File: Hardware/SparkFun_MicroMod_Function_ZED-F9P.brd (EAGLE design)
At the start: 38 x 65 mm, 112 parts, among them J1 USB Female Type C Connector, J10 U.FL, J11 455-1750-1-ND, J15 QWIIC_VERT, J16 QWIIC_RA, J18 Bus Selection, J2 MICROMOD_STANDARD, J3 Bus Selection, Q1 DMP21D0UT, U1 SN74LVC1G66DRYR, U10 SN74AUP1T04DCK, U11 SN74AUP1T04DCK, U2 3.3V, U3 EEPROM, U4 74LVC4066D_QUAD_BILATERAL_SWI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, U5 74LVC4066D_QUAD_BILATERAL_SWI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, U6 OPA344, U7 74LVC541ABQ, U8 U-BLOX_ZED-F9P, U9 FIN1017MXSOIC-8

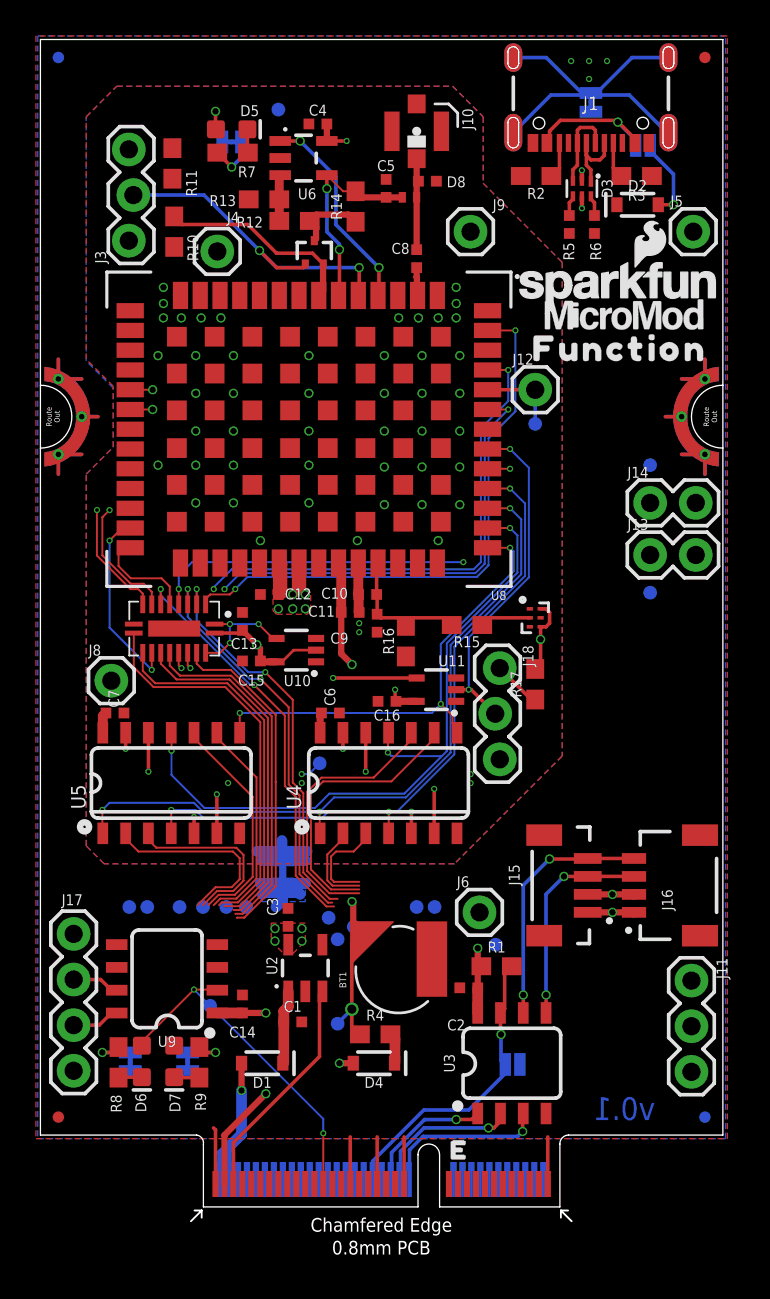
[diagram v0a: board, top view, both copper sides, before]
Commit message: All traces routed.
All traces routed, now need to just finish up via stitching, grounding, then silks.
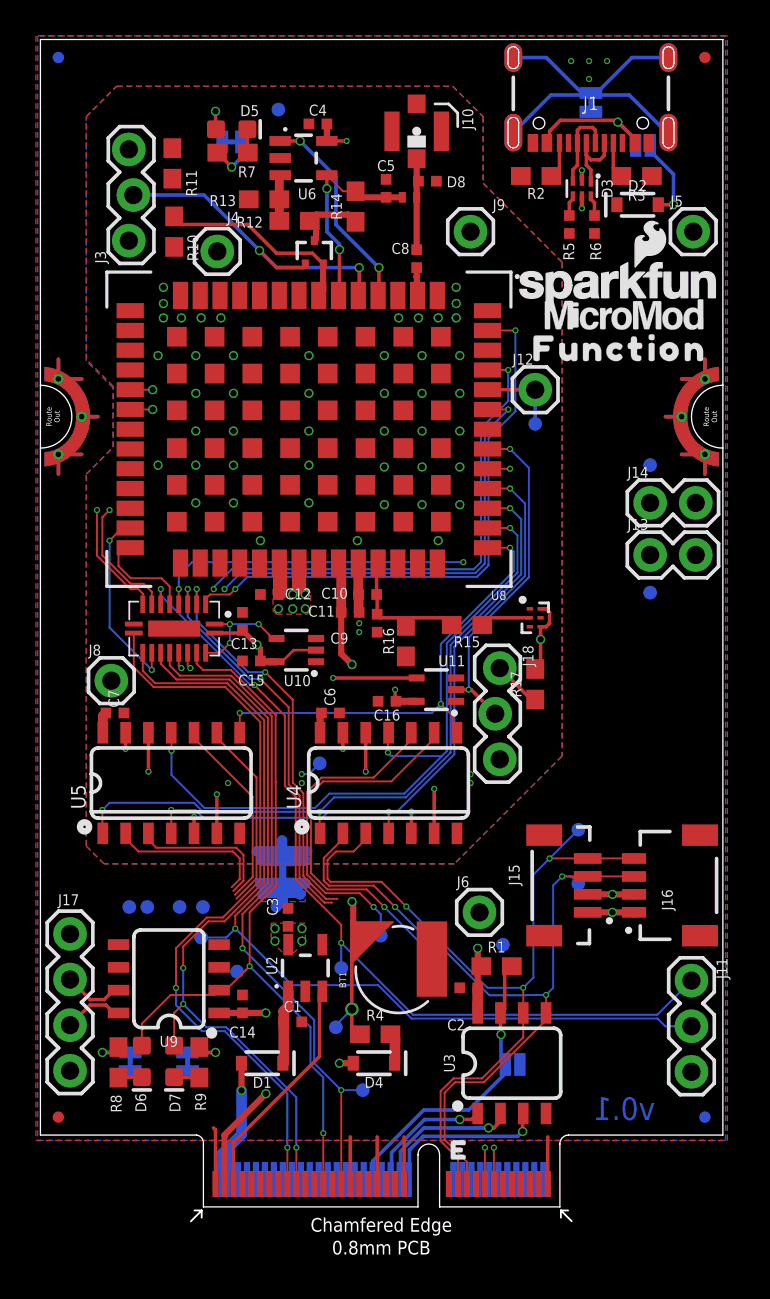
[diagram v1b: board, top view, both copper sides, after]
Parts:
- BT1: value ML414H_IV01E_BATTERY -> RELOWABLE_BATTERY_MS421R; device SparkFun-Batteries:ML414H_IV01E -> SparkFun-Batteries:MS421R_IV03E
- moved TP6 14.0 mm to (30.0, 18.0)
- moved TP5 13.6 mm to (30.0, 21.0)
- moved TP14 8.52 mm to (18.0, 6.50)
- moved TP15 7.25 mm to (16.8, 13.3)
- moved TP8 3.10 mm to (22.1, 13.6)
- moved TP16 3.02 mm to (9.00, 15.0)
- moved TP7 2.56 mm to (19.0, 15.1)
- moved TP9 2.42 mm to (11.0, 13.1)
- moved TP2 0.40 mm to (25.8, 14.6)
- moved TP3 0.22 mm to (16.5, 10.0)
- moved J17 0.20 mm to (1.70, 15.2)
- moved U9 0.10 mm to (7.20, 12.7)
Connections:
- net GEO_STAT: now also J2.59; no longer J2.57
- net RTK_STAT: now also J2.57; no longer J2.59
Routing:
- net TX2/RTCM: track 19.6 -> 50.1 mm, vias 0 -> 1
- net MM_SDA: track 16.8 -> 44.5 mm, vias 2 -> 3
- net MM_SCL: track 19.3 -> 46.3 mm, vias 2 -> 3
- net RX2/RTCM: track 22.9 -> 48.2 mm, vias 2 -> 3
- net MM_TX: track 15.8 -> 40.4 mm, vias 0 -> 2
- net RTK_STAT: track 20.7 -> 42.9 mm, vias 0 -> 3
- net MM_RX: track 15.2 -> 36.9 mm, vias 0 -> 2
- net GEO_STAT: track 21.9 -> 41.7 mm, vias 0 -> 2
- net TX_READY: track 19.6 -> 37.8 mm, vias 0 -> 2
- net PPS: track 38.1 -> 44.0 mm
- net MM_!CS!: track 11.2 -> 8.90 mm
- net MM_SCK: track 10.3 -> 8.25 mm
- net MM_COPI: track 12.5 -> 10.8 mm
- net MM_CIPO: track 12.0 -> 10.6 mm
- net PPS_DIFF_P: track 2.65 -> 3.38 mm
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
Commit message: Change net class for vbatt.
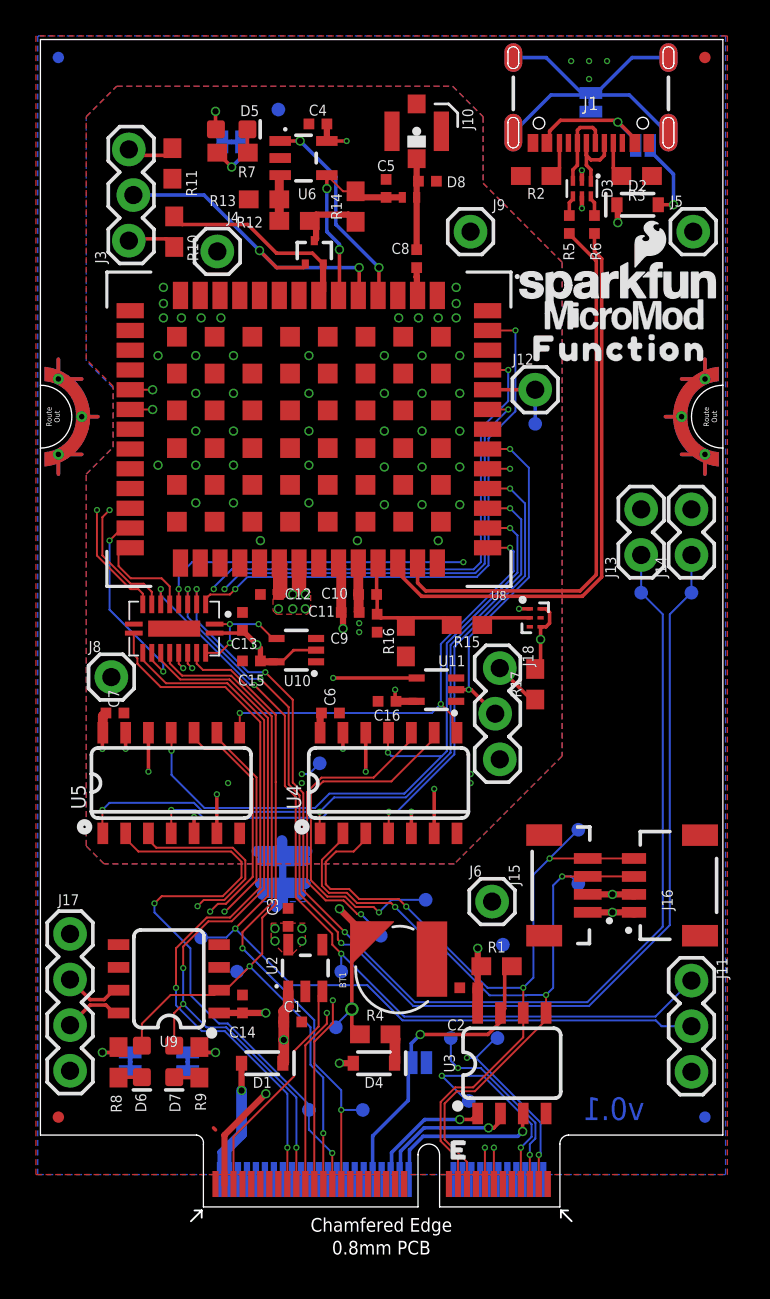
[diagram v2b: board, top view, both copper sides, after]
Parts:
- moved TP10 20.8 mm to (25.5, 9.40)
- moved TP13 18.3 mm to (23.9, 5.90)
- moved TP12 16.8 mm to (22.9, 9.40)
- moved TP11 15.1 mm to (15.0, 5.40)
- moved TP19 7.46 mm to (36.3, 34.2)
- moved JP2 5.20 mm to (21.1, 8.03)
- moved J14 3.70 mm to (36.3, 36.3), turned to 90 degrees
- moved TP8 3.55 mm to (21.5, 17.1)
- moved TP14 1.10 mm to (18.0, 5.40)
- moved J6 0.92 mm to (25.2, 17.0)
- moved J13 0.50 mm to (33.5, 36.3), turned to 90 degrees
- moved TP18 0.50 mm to (33.5, 34.2)
- moved TP15 0.20 mm to (16.8, 13.1)
- moved J8 0.20 mm to (4.00, 29.5)
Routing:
- net EXTINT: track 22.3 -> 81.8 mm, vias 2 -> 4
- net 5V: track 4.12 -> 63.2 mm, vias 0 -> 2
- net !RESET!: track 22.3 -> 81.2 mm, vias 2 -> 4
- net MM_SCK: track 8.25 -> 44.5 mm, vias 0 -> 3
- net MM_COPI: track 10.8 -> 44.8 mm, vias 0 -> 3
- net ZED_USB_N: track 0.00 -> 32.2 mm
- net MM_CIPO: track 10.6 -> 42.2 mm, vias 0 -> 3
- net ZED_USB_P: track 0.00 -> 31.2 mm
- net V_USB: track 14.4 -> 41.0 mm, vias 2 -> 3
- net MM_!CS!: track 8.90 -> 33.6 mm, vias 0 -> 2
- net GND: track 23.0 -> 9.49 mm
- net N$11: track 0.00 -> 2.75 mm
- net N$12: track 0.00 -> 2.73 mm
- net MM_TX: track 40.4 -> 38.5 mm
- net MM_RX: track 36.9 -> 35.7 mm
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
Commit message: GND stitching and grounding complete.
Outer GND plane stitching complete.
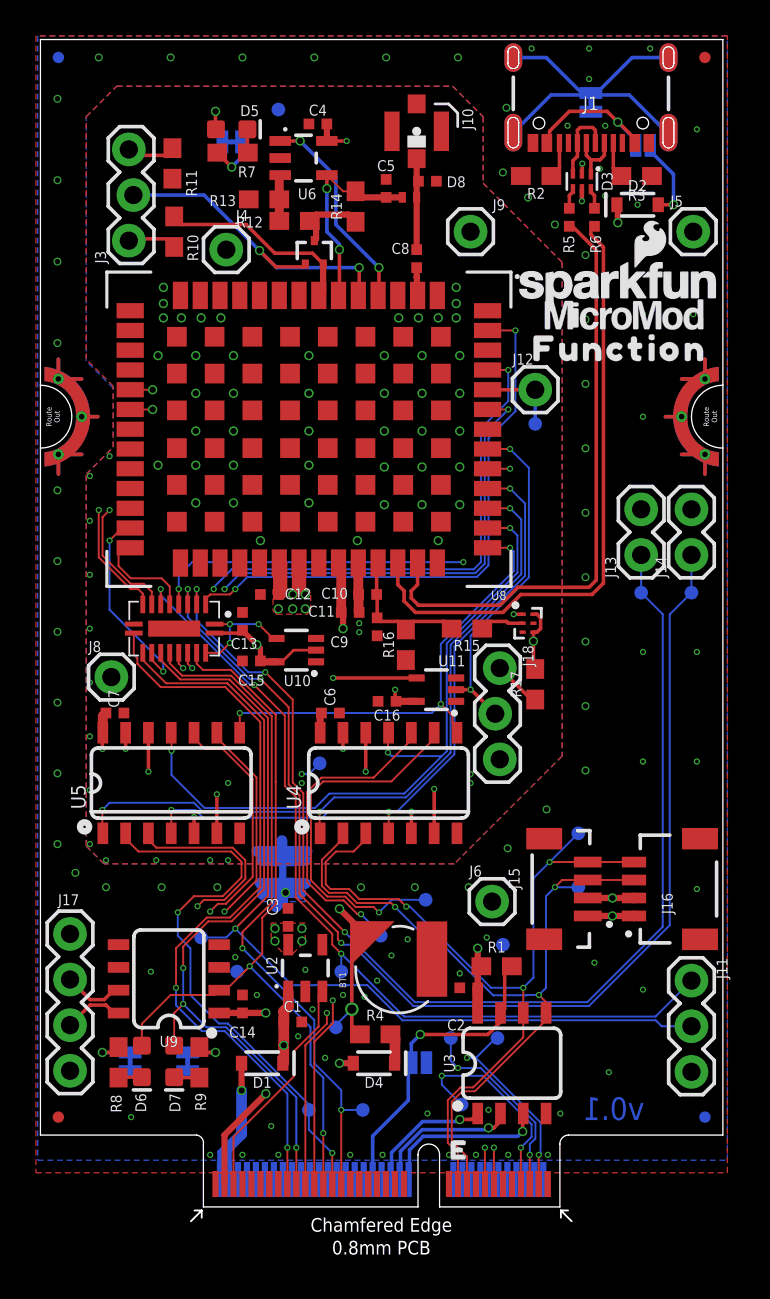
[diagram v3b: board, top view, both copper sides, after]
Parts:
- moved J4 0.51 mm to (10.4, 53.3)
- moved U1 0.50 mm to (26.9, 33.0)
- moved TP13 0.45 mm to (23.5, 5.70)
- moved D3 0.40 mm to (30.2, 57.1)
- moved R5 0.40 mm to (29.5, 55.1)
- moved R6 0.40 mm to (30.9, 55.1)
- moved C9 0.20 mm to (18.8, 32.3)
- moved J15 0.20 mm to (31.3, 17.7)
- moved J16 0.20 mm to (33.1, 17.7)
- moved R16 0.20 mm to (20.4, 31.3)
- moved TP5 0.20 mm to (30.0, 20.8)
- moved TP6 0.20 mm to (30.0, 17.8)
- moved R15 0.20 mm to (23.8, 32.2)
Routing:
- net ZED_USB_N: track 32.2 -> 34.5 mm
- net ZED_USB_P: track 31.2 -> 33.6 mm
- net MM_!CS!: track 33.6 -> 31.5 mm
- net USBC_N: track 4.83 -> 3.38 mm
- net V_USB: track 41.0 -> 42.2 mm
- net MM_SCL: track 46.3 -> 45.6 mm
- net V_ZED: track 24.4 -> 23.8 mm
- net MM_SDA: track 44.4 -> 43.9 mm
- net GND: track 9.49 -> 9.32 mm, vias 6 -> 88
- net GND_RF: vias 49 -> 62

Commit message: Stitching of GND_RF complete.
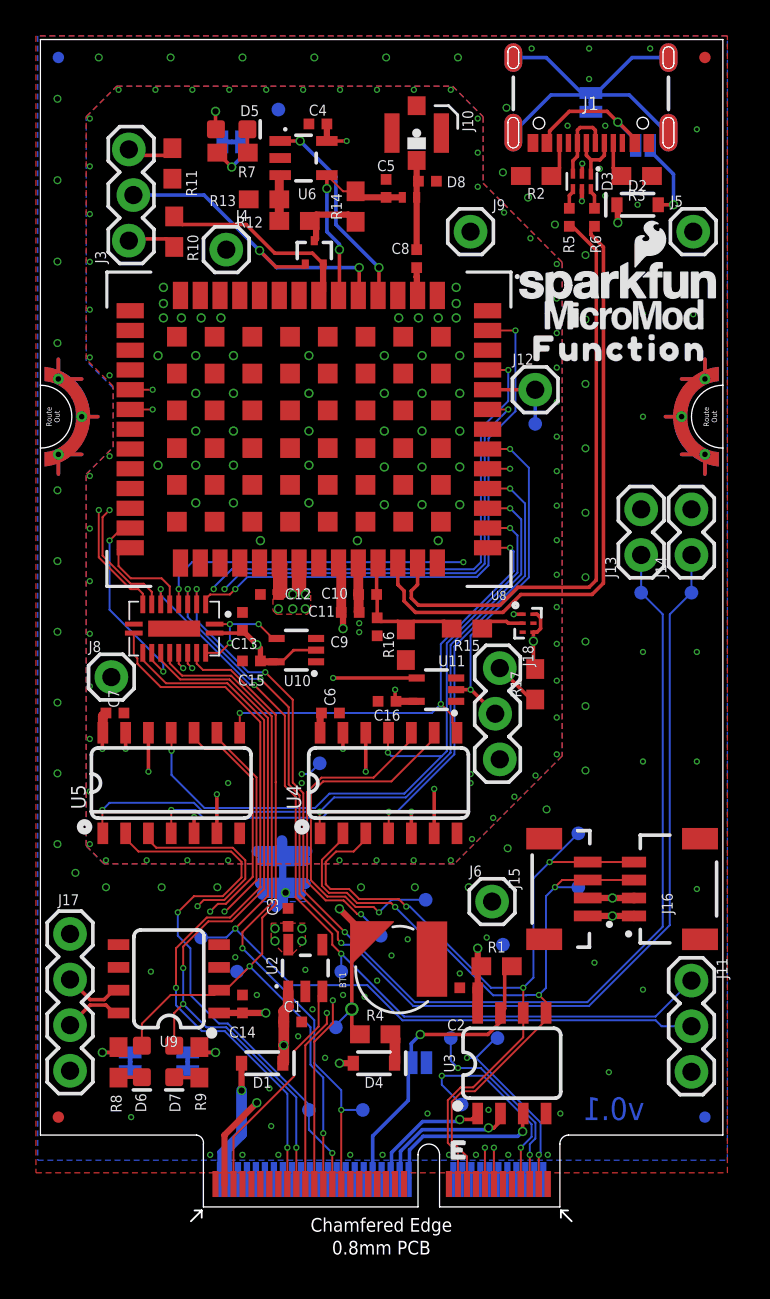
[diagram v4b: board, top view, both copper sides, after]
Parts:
- moved J10 0.10 mm to (21.0, 59.8)
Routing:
- net 3.3V: track 44.3 -> 45.9 mm
- net GND_RF: vias 62 -> 107
- net GND: vias 88 -> 89
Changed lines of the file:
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@@
 <attribute name="VALUE" x="18.362" y="55.7" size="0.6096" layer="27" font="vector" ratio="20" rot="R90" align="top-center"/>
 </element>
-<element name="J10" library="SparkFun-Connectors" package="U.FL" value="U.FL" x="21" y="59.89" smashed="yes" rot="R270">
-<attribute name="NAME" x="23.54" y="61.16" size="0.6096" layer="25" font="vector" ratio="20" rot="R270"/>
-<attribute name="PROD_ID" value="CONN-09193" x="21" y="59.89" size="1.778" layer="27" rot="R270" display="off"/>
-<attribute name="SF_ID" value="WRL-09144" x="21" y="59.89" size="1.778" layer="27" rot="R270" display="off"/>
-<attribute name="VALUE" x="18.46" y="61.16" size="0.6096" layer="27" font="vector" ratio="20" rot="R270" align="top-left"/>
+<element name="J10" library="SparkFun-Connectors" package="U.FL" value="U.FL" x="21" y="59.79" smashed="yes" rot="R270">
+<attribute name="NAME" x="23.54" y="61.06" size="0.6096" layer="25" font="vector" ratio="20" rot="R270"/>
+<attribute name="PROD_ID" value="CONN-09193" x="21" y="59.79" size="1.778" layer="27" rot="R270" display="off"/>
+<attribute name="SF_ID" value="WRL-09144" x="21" y="59.79" size="1.778" layer="27" rot="R270" display="off"/>
+<attribute name="VALUE" x="18.46" y="61.06" size="0.6096" layer="27" font="vector" ratio="20" rot="R270" align="top-left"/>
 </element>
 <element name="D8" library="SparkFun-DiscreteSemi" package="0402-TIGHT" value="PESD0402-0402T" x="21.6" y="57.11" smashed="yes">
@@
 <via x="21.6" y="5.2" extent="1-16" drill="0.2"/>
 <via x="25" y="5.4" extent="1-16" drill="0.2"/>
+<via x="12.8" y="6.6" extent="1-16" drill="0.2"/>
 </signal>
 <signal name="3.3V" class="4">
@@
 <wire x1="31.9" y1="17.2" x2="29.1" y2="14.4" width="0.35" layer="15"/>
 <wire x1="10.3" y1="1.275" x2="10.3" y2="4" width="0.35" layer="1"/>
-<wire x1="10.3" y1="4" x2="12.6" y2="6.3" width="0.35" layer="1"/>
-<via x="12.6" y="6.3" extent="1-16" drill="0.35"/>
-<wire x1="16.7" y1="8" x2="15" y2="6.3" width="0.35" layer="15"/>
-<wire x1="12.6" y1="6.3" x2="15" y2="6.3" width="0.35" layer="15"/>
-<wire x1="12.6" y1="6.3" x2="12.6" y2="10.8" width="0.35" layer="15"/>
+<wire x1="10.3" y1="4" x2="12.1" y2="5.8" width="0.35" layer="1"/>
+<via x="12.1" y="5.8" extent="1-16" drill="0.35"/>
+<wire x1="16.7" y1="8" x2="16.7" y2="6.4" width="0.35" layer="15"/>
+<wire x1="16.7" y1="6.4" x2="16.1" y2="5.8" width="0.35" layer="15"/>
+<wire x1="12.1" y1="5.8" x2="16.1" y2="5.8" width="0.35" layer="15"/>
+<wire x1="12.1" y1="10.3" x2="12.6" y2="10.8" width="0.35" layer="15"/>
+<wire x1="12.1" y1="10.3" x2="12.1" y2="5.8" width="0.35" layer="15"/>
 <via x="12.6" y="10.8" extent="1-16" drill="0.35"/>
 <wire x1="12.6" y1="10.8" x2="11.3" y2="10.8" width="0.35" layer="1"/>
@@
 <wire x1="3.51" y1="36.26346875" x2="5.07506875" y2="34.6984" width="0.11" layer="1"/>
 <wire x1="5.05" y1="44.4" x2="6.3" y2="44.4" width="0.11" layer="1"/>
-<via x="6.3" y="44.4" extent="1-16" drill="0.35"/>
+<via x="6.3" y="44.4" extent="1-16" drill="0.2"/>
 <wire x1="6.3" y1="44.4" x2="5.8116" y2="43.9116" width="0.11" layer="15"/>
 <wire x1="5.8116" y1="43.9116" x2="5.8116" y2="42.11235" width="0.11" layer="15"/>
@@
 <wire x1="5.75" y1="34.1468" x2="5.5" y2="34.3968" width="0.11" layer="1"/>
 <wire x1="5.05" y1="45.5" x2="6.3" y2="45.5" width="0.11" layer="1"/>
-<via x="6.3" y="45.5" extent="1-16" drill="0.35"/>
+<via x="6.3" y="45.5" extent="1-16" drill="0.2"/>
 <wire x1="6.3" y1="45.5" x2="5.6" y2="44.8" width="0.11" layer="15"/>
 <wire x1="3.68" y1="40.28" x2="3.68" y2="39.18" width="0.11" layer="15"/>
@@
 <vertex x="24.7" y="60.7"/>
 </polygon>
-<via x="10.5" y="19.3" extent="1-16" drill="0.2"/>
-<via x="9.5" y="19.3" extent="1-16" drill="0.2"/>
-<via x="6.5" y="19.3" extent="1-16" drill="0.2"/>
+<via x="10.499996875" y="19.3" extent="1-16" drill="0.2"/>
+<via x="8.23333125" y="19.3" extent="1-16" drill="0.2"/>
+<via x="5.966665625" y="19.3" extent="1-16" drill="0.2"/>
 <via x="3.7" y="19.3" extent="1-16" drill="0.2"/>
 <via x="2.8" y="20.2" extent="1-16" drill="0.2"/>
-<via x="2.8" y="23.2" extent="1-16" drill="0.2"/>
-<via x="2.8" y="26.2" extent="1-16" drill="0.2"/>
-<via x="2.8" y="29.2" extent="1-16" drill="0.2"/>
-<via x="2.8" y="32.2" extent="1-16" drill="0.2"/>
-<via x="2.8" y="35.2" extent="1-16" drill="0.2"/>
-<via x="2.8" y="38.2" extent="1-16" drill="0.2"/>
-<via x="2.8" y="40.7" extent="1-16" drill="0.2"/>
+<via x="2.8" y="23.12856875" extent="1-16" drill="0.2"/>
+<via x="2.8" y="26.0571375" extent="1-16" drill="0.2"/>
+<via x="2.8" y="28.98570625" extent="1-16" drill="0.2"/>
+<via x="2.8" y="31.914275" extent="1-16" drill="0.2"/>
+<via x="2.8" y="34.84284375" extent="1-16" drill="0.2"/>
+<via x="2.8" y="37.7714125" extent="1-16" drill="0.2"/>
+<via x="2.8" y="40.69998125" extent="1-16" drill="0.2"/>
 <via x="3.9" y="41.8" extent="1-16" drill="0.2"/>
+<via x="3.9" y="46.3" extent="1-16" drill="0.2"/>
+<via x="2.8" y="47.3" extent="1-16" drill="0.2"/>
+<via x="2.8" y="49.96" extent="1-16" drill="0.2"/>
+<via x="2.8" y="52.62" extent="1-16" drill="0.2"/>
+<via x="2.8" y="55.28" extent="1-16" drill="0.2"/>
+<via x="2.8" y="57.94" extent="1-16" drill="0.2"/>
+<via x="2.8" y="60.6" extent="1-16" drill="0.2"/>
+<via x="4.4" y="62.2" extent="1-16" drill="0.2"/>
+<via x="6.45555" y="62.2" extent="1-16" drill="0.2"/>
+<via x="8.5111" y="62.2" extent="1-16" drill="0.2"/>
+<via x="10.56665" y="62.2" extent="1-16" drill="0.2"/>
+<via x="12.6222" y="62.2" extent="1-16" drill="0.2"/>
+<via x="14.67775" y="62.2" extent="1-16" drill="0.2"/>
+<via x="16.7333" y="62.2" extent="1-16" drill="0.2"/>
+<via x="22.89995" y="62.2" extent="1-16" drill="0.2"/>
+<via x="18.78885" y="62.2" extent="1-16" drill="0.2"/>
+<via x="20.8444" y="62.2" extent="1-16" drill="0.2"/>
+<via x="24.4" y="60.6" extent="1-16" drill="0.2"/>
+<via x="24.4" y="58.7" extent="1-16" drill="0.2"/>
+<via x="24.4" y="56.79999375" extent="1-16" drill="0.2"/>
+<via x="28.799996875" y="52.499996875" extent="1-16" drill="0.2"/>
+<via x="27.33333125" y="53.93333125" extent="1-16" drill="0.2"/>
+<via x="25.866665625" y="55.3666625" extent="1-16" drill="0.2"/>
+<via x="28.799996875" y="50.577775" extent="1-16" drill="0.2"/>
+<via x="28.799996875" y="48.655553125" extent="1-16" drill="0.2"/>
+<via x="28.799996875" y="46.73333125" extent="1-16" drill="0.2"/>
+<via x="28.799996875" y="44.811109375" extent="1-16" drill="0.2"/>
+<via x="28.799996875" y="42.8888875" extent="1-16" drill="0.2"/>
+<via x="28.799996875" y="40.966665625" extent="1-16" drill="0.2"/>
+<via x="28.799996875" y="39.04444375" extent="1-16" drill="0.2"/>
+<via x="28.799996875" y="37.122221875" extent="1-16" drill="0.2"/>
+<via x="28.799996875" y="35.2" extent="1-16" drill="0.2"/>
+<via x="28.799996875" y="33.4" extent="1-16" drill="0.2"/>
+<via x="28.799996875" y="31.35" extent="1-16" drill="0.2"/>
+<via x="28.799996875" y="29.3" extent="1-16" drill="0.2"/>
+<via x="28.799996875" y="25.2" extent="1-16" drill="0.2"/>
+<via x="28.799996875" y="27.25" extent="1-16" drill="0.2"/>
+<via x="22.89999375" y="19.3" extent="1-16" drill="0.2"/>
+<via x="24.079996875" y="20.48" extent="1-16" drill="0.2"/>
+<via x="25.259996875" y="21.66" extent="1-16" drill="0.2"/>
+<via x="26.439996875" y="22.84" extent="1-16" drill="0.2"/>
+<via x="27.619996875" y="24.02" extent="1-16" drill="0.2"/>
+<via x="16.699996875" y="19.3" extent="1-16" drill="0.2"/>
+<via x="18.7666625" y="19.3" extent="1-16" drill="0.2"/>
+<via x="20.833328125" y="19.3" extent="1-16" drill="0.2"/>
 <wire x1="11.3" y1="33.1" x2="11.3" y2="30.4" width="0" layer="19" extent="1-1"/>
 </signal>
@@
 <wire x1="21" y1="57.01" x2="21.1" y2="57.11" width="0.35" layer="1"/>
 <wire x1="21.1" y1="57.11" x2="21" y2="57.21" width="0.35" layer="1"/>
-<wire x1="21" y1="57.21" x2="21" y2="58.365" width="0.35" layer="1"/>
+<wire x1="21" y1="57.21" x2="21" y2="58.265" width="0.35" layer="1"/>
 <wire x1="21" y1="53.3" x2="21" y2="56.21" width="0.35" layer="1"/>
 </signal>

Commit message: Passed DRC.
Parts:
- moved R13 0.20 mm to (12.5, 56.3)
- moved C12 0.14 mm to (12.7, 34.0)
- moved C13 0.14 mm to (11.2, 32.5)
- moved J12 0.14 mm to (27.7, 45.6)
- moved R12 0.10 mm to (14.2, 54.8)
- moved TP17 0.10 mm to (27.7, 43.6)
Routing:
- net V_ZED: track 23.8 -> 25.7 mm
- net SHLD: track 20.3 -> 18.7 mm
- net N$14: track 6.71 -> 7.90 mm
- net GND: track 9.32 -> 8.47 mm
- net !ZED_DSEL!: track 28.2 -> 27.9 mm, vias 6 -> 5
- net GND_RF: vias 107 -> 155
